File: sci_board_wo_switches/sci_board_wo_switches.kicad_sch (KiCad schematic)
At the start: 18 parts

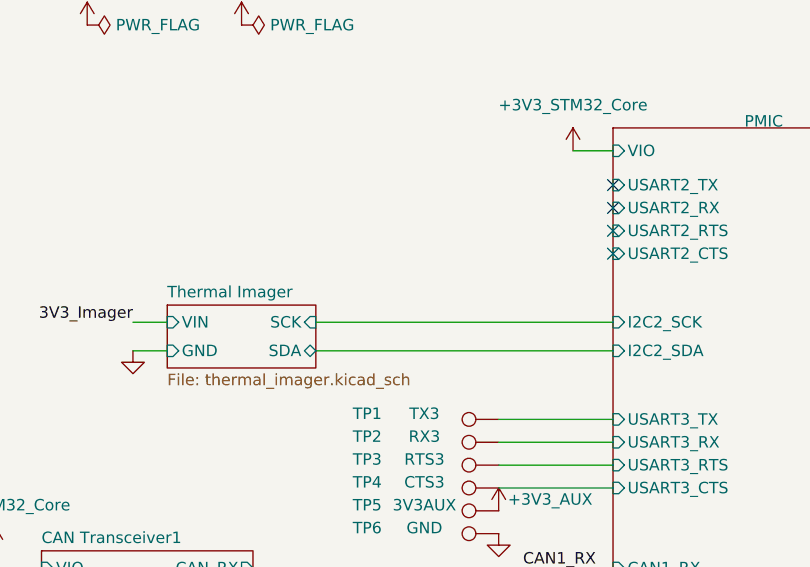
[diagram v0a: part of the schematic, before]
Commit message: bom for SCI
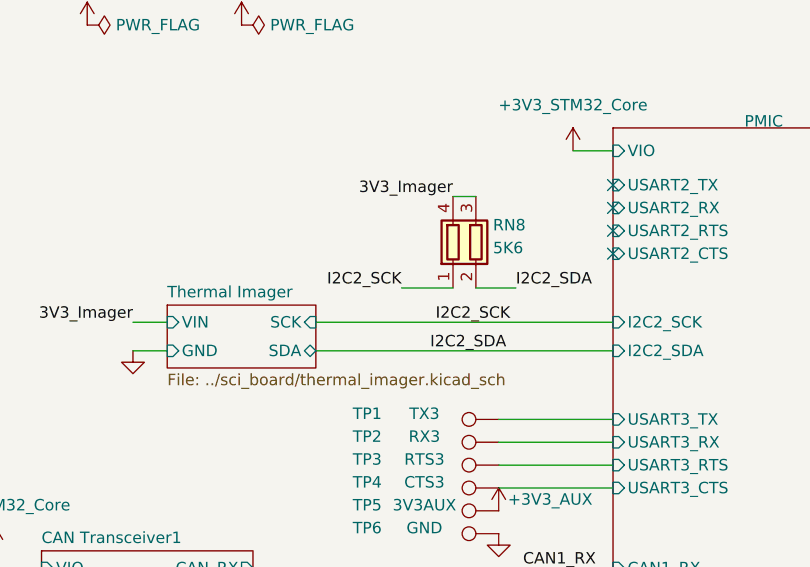
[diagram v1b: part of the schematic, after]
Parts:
- added RN8: 5K6, Resistor_SMD:R_Array_Convex_2x0402, symbol Device:R_Pack02
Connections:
- net 3V3_Imager: now also RN8.3 (R2.2), RN8.4 (R1.2)
- new net I2C2_SCK: RN8.1 (R1.1)
- new net I2C2_SDA: RN8.2 (R2.1)
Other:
- sheet Thermal Imager: file thermal_imager.kicad_sch -> ../sci_board/thermal_imager.kicad_sch
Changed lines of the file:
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@@
 	(wire
 		(pts
+			(xy 64.77 49.53) (xy 70.485 49.53)
+		)
+		(stroke
+			(width 0)
+			(type default)
+		)
+	)
+	(wire
+		(pts
+			(xy 77.47 49.53) (xy 73.025 49.53)
+		)
+		(stroke
+			(width 0)
+			(type default)
+		)
+	)
+	(wire
+		(pts
 			(xy 126.365 105.41) (xy 177.165 105.41)
 		)
@@
 	(wire
 		(pts
+			(xy 70.485 39.37) (xy 73.025 39.37)
+		)
+		(stroke
+			(width 0)
+			(type default)
+		)
+	)
+	(wire
+		(pts
 			(xy 48.26 88.265) (xy 88.265 88.265)
 		)
@@
 		)
 	)
+	(label "I2C2_SCK"
+		(at 76.835 53.34 180)
+		(effects
+			(font
+				(size 1.27 1.27)
+			)
+			(justify right bottom)
+		)
+	)
 	(label "3V3_Cameras"
 		(at 155.575 64.135 180)
@@
 		)
 	)
+	(label "I2C2_SDA"
+		(at 67.945 56.515 0)
+		(effects
+			(font
+				(size 1.27 1.27)
+			)
+			(justify left bottom)
+		)
+	)
 	(label "CAN2_STB"
 		(at 86.36 106.68 180)
@@
 		)
 	)
+	(label "I2C2_SCK"
+		(at 64.77 49.53 180)
+		(effects
+			(font
+				(size 1.27 1.27)
+			)
+			(justify right bottom)
+		)
+	)
 	(label "3V3_Imager"
 		(at 34.925 128.27 180)
@@
 		)
 	)
+	(label "3V3_Imager"
+		(at 70.485 39.37 180)
+		(effects
+			(font
+				(size 1.27 1.27)
+			)
+			(justify right bottom)
+		)
+	)
 	(label "CAN2_H"
 		(at 22.225 109.855 180)
@@
 		)
 	)
+	(label "I2C2_SDA"
+		(at 77.47 49.53 0)
+		(effects
+			(font
+				(size 1.27 1.27)
+			)
+			(justify left bottom)
+		)
+	)
 	(symbol
 		(lib_id "power:+3V3")
@@
 	)
 	(symbol
+		(lib_id "Device:R_Pack02")
+		(at 73.025 44.45 0)
+		(unit 1)
+		(exclude_from_sim no)
+		(in_bom yes)
+		(on_board yes)
+		(dnp no)
+		(property "Reference" "RN8"
+			(at 74.93 42.545 0)
+			(effects
+				(font
+					(size 1.27 1.27)
+				)
+				(justify left)
+			)
+		)
+		(property "Value" "5K6"
+			(at 74.93 45.085 0)
+			(effects
+				(font
+					(size 1.27 1.27)
+				)
+				(justify left)
+			)
+		)
+		(property "Footprint" "Resistor_SMD:R_Array_Convex_2x0402"
+			(at 77.47 44.45 90)
+			(effects
+				(font
+					(size 1.27 1.27)
+				)
+				(hide yes)
+			)
+		)
+		(property "Datasheet" "~"
+			(at 73.025 44.45 0)
+			(effects
+				(font
+					(size 1.27 1.27)
+				)
+				(hide yes)
+			)
+		)
+		(property "Description" "2 resistor network, parallel topology"
+			(at 73.025 44.45 0)
+			(effects
+				(font
+					(size 1.27 1.27)
+				)
+				(hide yes)
+			)
+		)
+		(pin "3"
+		)
+		(pin "1"
+		)
+		(pin "4"
+		)
+		(pin "2"
+		)
+		(instances
+			(project "sci_board_wo_switches"
+				(path "/b4b2c88d-f6cd-4e60-862d-e21f68728580"
+					(reference "RN8")
+					(unit 1)
+				)
+			)
+		)
+	)
+	(symbol
 		(lib_id "power:GND")
 		(at 168.275 154.305 0)
@@
 			)
 		)
-		(property "Sheetfile" "thermal_imager.kicad_sch"
+		(property "Sheetfile" "../sci_board/thermal_imager.kicad_sch"
 			(at 38.735 59.0046 0)
 			(effects

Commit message: EPS AVI SCI SCIwoSwitches RF AUX all updated to use RNs. BOMs completed
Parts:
- R1, R2: MANUFACTURER YAGEO -> (none); Manufacturer (none) -> YAGEO; PARTREV RC0402FR-0710KL -> (none); Part Number (none) -> RC0402FR-0710KL
- R3: MANUFACTURER YAGEO -> (none); Manufacturer (none) -> YAGEO; PARTREV RC0402FR-0722RL -> (none); Part Number (none) -> RC0402FR-0722RL
- R4: MANUFACTURER YAGEO -> (none); Manufacturer (none) -> YAGEO; PARTREV RC0402FR-07100KL -> (none); Part Number (none) -> RC0402FR-07100KL
- R5: MANUFACTURER YAGEO -> (none); Manufacturer (none) -> YAGEO; PARTREV RC0402FR-07330KL -> (none); Part Number (none) -> RC0402FR-07330KL
- RN1, RN3, RN8: Manufacturer (none) -> Panasonic; Part Number (none) -> EXB-24V562JX; Tolerance (none) -> 5
- RN2: Manufacturer (none) -> Panasonic; Part Number (none) -> EXB-24V220JX; Tolerance (none) -> 5
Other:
- sheet Aux Power Switch 3V3: file i2c_aux_power_switch.kicad_sch -> ../sci_board/i2c_aux_power_switch.kicad_sch
- sheet Flash1: file flash.kicad_sch -> ../sci_board/flash.kicad_sch
- sheet Flash2: file flash.kicad_sch -> ../sci_board/flash.kicad_sch

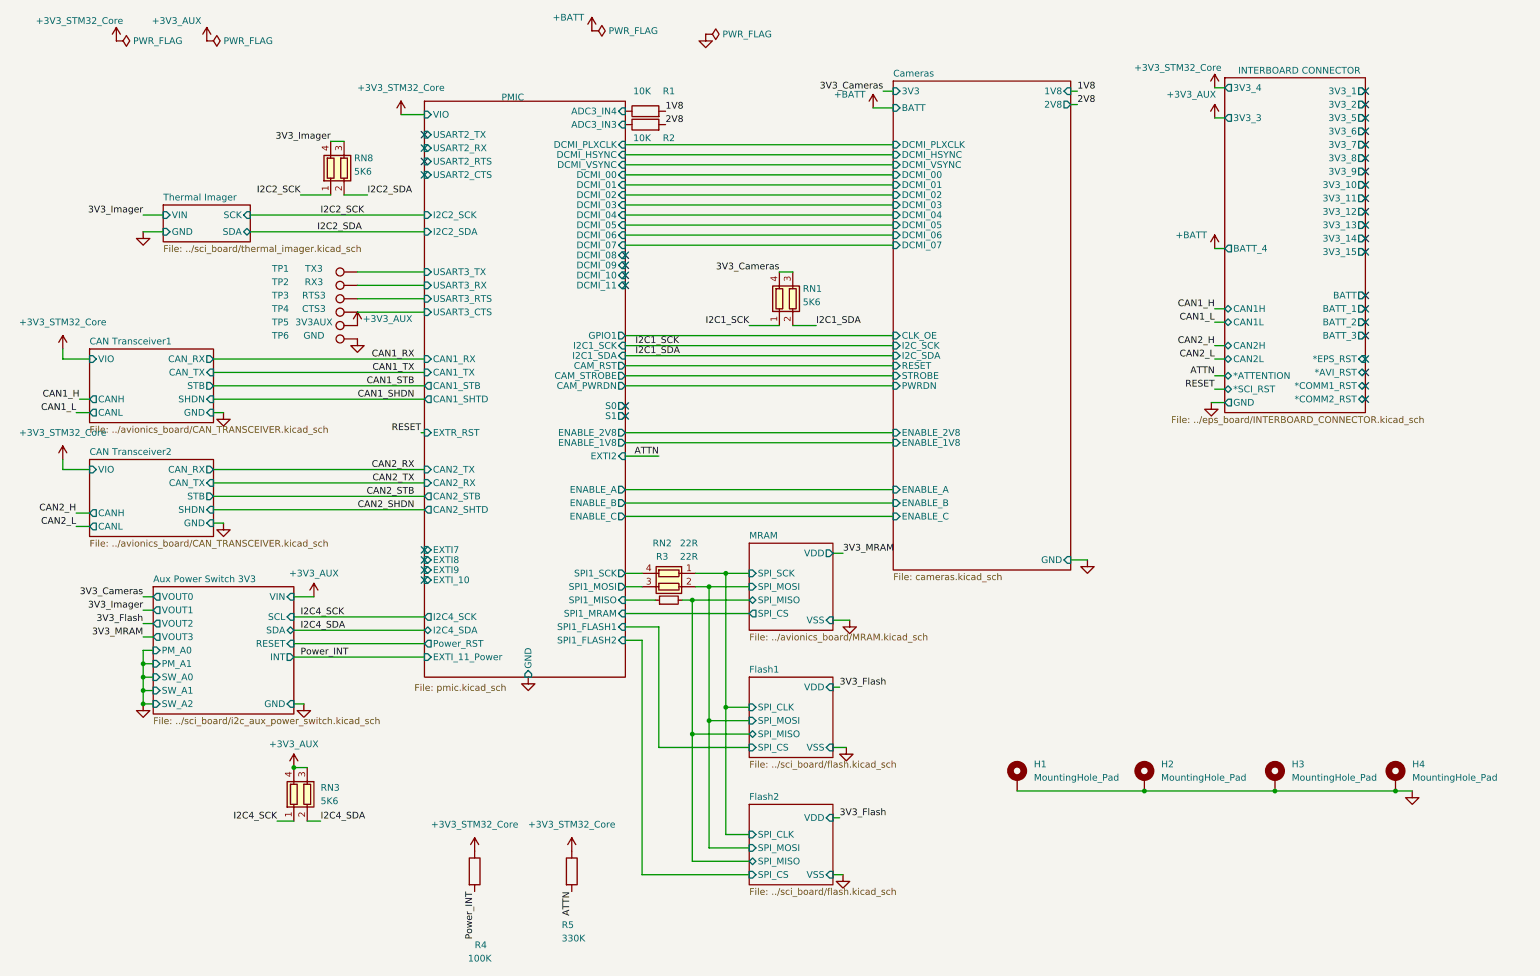
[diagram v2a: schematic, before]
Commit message: sorting out pullups on resets and attention. replace reset with RN where possible. Introduce CN to save some parts
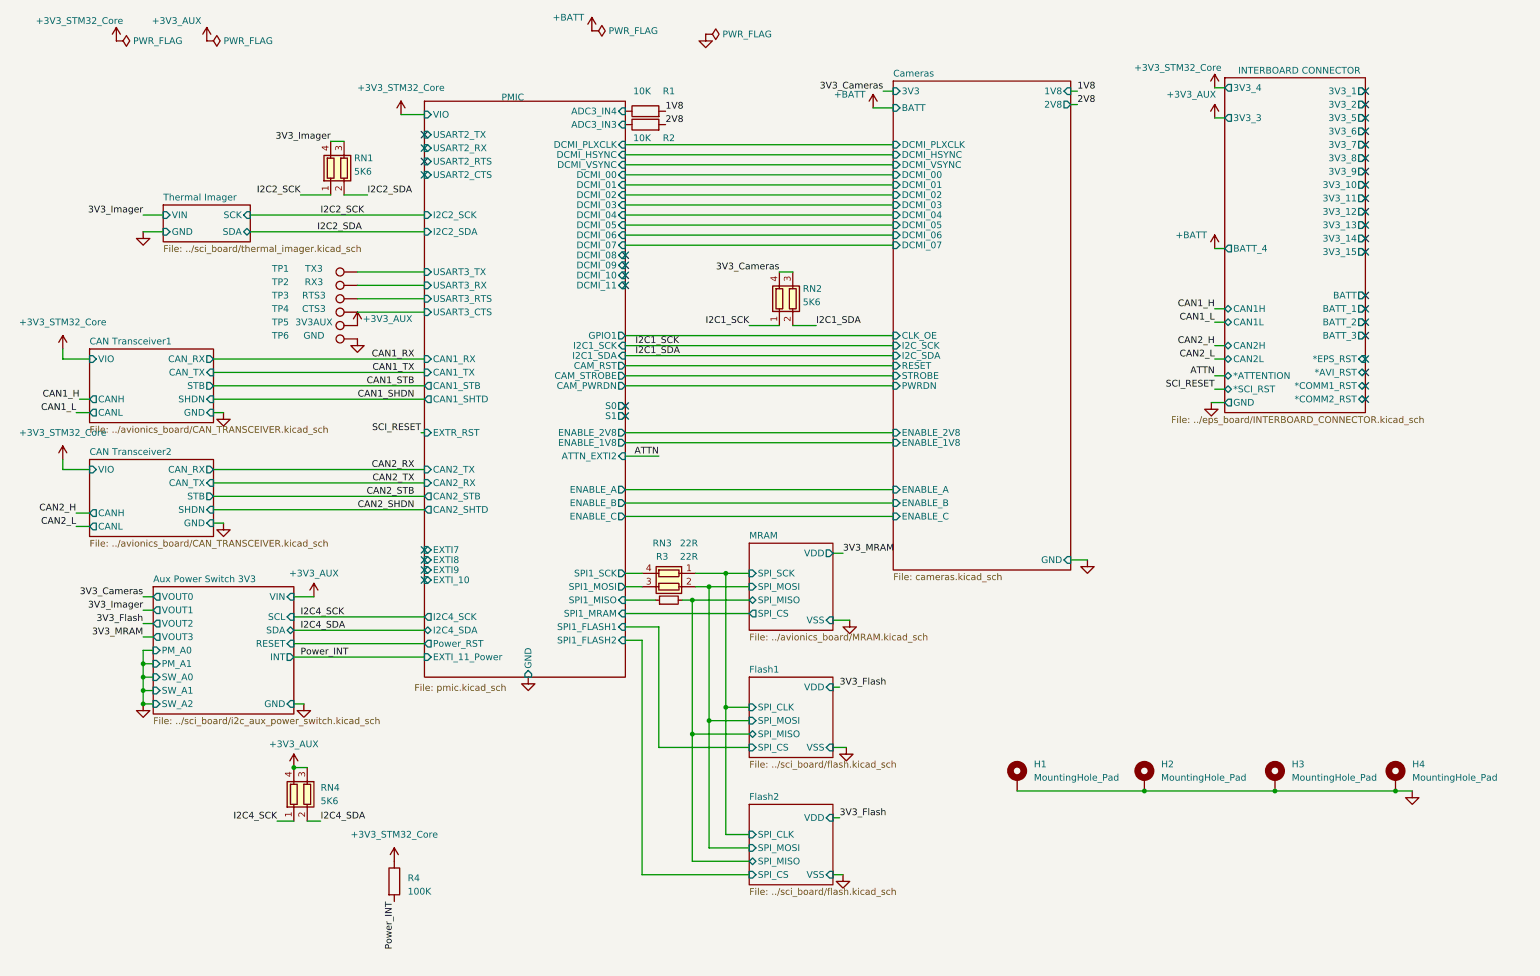
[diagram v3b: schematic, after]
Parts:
- removed R5: 330K, Resistor_SMD:R_0402_1005Metric_Pad0.72x0.64mm_HandSolder, symbol Device:R
- renumbered RN8 to RN1, RN1 to RN2, RN2 to RN3, RN3 to RN4
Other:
- sheet PMIC ports: added ATTN_EXTI2; removed EXTI2
- moved on the sheet: R4
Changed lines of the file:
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@@
 		)
 	)
-	(label "ATTN"
-		(at 116.205 181.61 270)
-		(effects
-			(font
-				(size 1.27 1.27)
-			)
-			(justify right bottom)
-		)
-	)
 	(label "Power_INT"
-		(at 97.79 181.61 270)
+		(at 82.55 183.515 270)
 		(effects
 			(font
@@
 		)
 	)
-	(label "RESET"
+	(label "SCI_RESET"
 		(at 87.63 94.615 180)
 		(effects
@@
 		)
 	)
-	(label "RESET"
+	(label "SCI_RESET"
 		(at 238.125 86.36 180)
 		(effects
@@
 	(symbol
 		(lib_id "Device:R")
-		(at 97.79 177.8 0)
+		(at 82.55 179.705 0)
 		(unit 1)
 		(exclude_from_sim no)
@@
 		(dnp no)
 		(property "Reference" "R4"
-			(at 97.79 191.77 0)
+			(at 85.09 179.07 0)
 			(effects
 				(font
@@
 		)
 		(property "Value" "100K"
-			(at 96.52 194.31 0)
+			(at 85.09 181.61 0)
 			(effects
 				(font
@@
 		)
 		(property "Footprint" "Resistor_SMD:R_0402_1005Metric_Pad0.72x0.64mm_HandSolder"
-			(at 96.012 177.8 90)
+			(at 80.772 179.705 90)
 			(effects
 				(font
@@
 		)
 		(property "Datasheet" "https://www.yageo.com/upload/media/product/app/datasheet/rchip/pyu-rt_1-to-0.01_rohs_l.pdf"
-			(at 97.79 177.8 0)
+			(at 82.55 179.705 0)
 			(effects
 				(font
@@
 		)
 		(property "Description" "Resistor"
-			(at 97.79 177.8 0)
+			(at 82.55 179.705 0)
 			(effects
 				(font
@@
 		)
 		(property "Note" "pullup/pulldown"
-			(at 97.79 177.8 0)
+			(at 82.55 179.705 0)
 			(effects
 				(font
@@
 		)
 		(property "Tolerance" "1"
-			(at 97.79 177.8 0)
+			(at 82.55 179.705 0)
 			(effects
 				(font
@@
 		)
 		(property "Manufacturer" "YAGEO"
-			(at 97.79 177.8 0)
+			(at 82.55 179.705 0)
 			(effects
 				(font
@@
 		)
 		(property "Part Number" "RC0402FR-07100KL"
-			(at 97.79 177.8 0)
+			(at 82.55 179.705 0)
 			(effects
 				(font
@@
 		(dnp no)
 		(fields_autoplaced yes)
-		(property "Reference" "RN3"
+		(property "Reference" "RN4"
 			(at 68.58 161.9249 0)
 			(effects
@@
 			(project ""
 				(path "/b4b2c88d-f6cd-4e60-862d-e21f68728580"
-					(reference "RN3")
+					(reference "RN4")
 					(unit 1)
 				)
@@
 		(dnp no)
 		(fields_autoplaced yes)
-		(property "Reference" "#PWR029"
+		(property "Reference" "#PWR028"
 			(at 167.64 184.785 0)
 			(effects
@@
 			(project "sci_board"
 				(path "/b4b2c88d-f6cd-4e60-862d-e21f68728580"
-					(reference "#PWR029")
+					(reference "#PWR028")
 					(unit 1)
 				)
@@
 		(on_board yes)
 		(dnp no)
-		(property "Reference" "RN2"
+		(property "Reference" "RN3"
 			(at 133.35 115.57 90)
 			(effects
@@
 			(project "sci_board"
 				(path "/b4b2c88d-f6cd-4e60-862d-e21f68728580"
-					(reference "RN2")
+					(reference "RN3")
 					(unit 1)
 				)
@@
 	(symbol
 		(lib_id "power:+3V3")
-		(at 97.79 173.99 0)
+		(at 82.55 175.895 0)
 		(unit 1)
 		(exclude_from_sim no)
@@
 		(fields_autoplaced yes)
 		(property "Reference" "#PWR027"
-			(at 97.79 177.8 0)
+			(at 82.55 179.705 0)
 			(effects
 				(font
@@
 		)
 		(property "Value" "+3V3_STM32_Core"
-			(at 97.79 168.91 0)
+			(at 82.55 170.815 0)
 			(effects
 				(font
@@
 		)
 		(property "Footprint" ""
-			(at 97.79 173.99 0)
+			(at 82.55 175.895 0)
 			(effects
 				(font
@@
 		)
 		(property "Datasheet" ""
-			(at 97.79 173.99 0)
+			(at 82.55 175.895 0)
 			(effects
 				(font
@@
 		)
 		(property "Description" "Power symbol creates a global label with name \"+3V3\""
-			(at 97.79 173.99 0)
+			(at 82.55 175.895 0)
 			(effects
 				(font
@@
 		(on_board yes)
 		(dnp no)
-		(property "Reference" "RN8"
+		(property "Reference" "RN1"
 			(at 74.93 42.545 0)
 			(effects
@@
 			(project "sci_board_wo_switches"
 				(path "/b4b2c88d-f6cd-4e60-862d-e21f68728580"
-					(reference "RN8")
+					(reference "RN1")
 					(unit 1)
 				)
@@
 		(on_board yes)
 		(dnp no)
-		(property "Reference" "RN1"
+		(property "Reference" "RN2"
 			(at 160.02 67.31 0)
 			(effects
@@
 			(project ""
 				(path "/b4b2c88d-f6cd-4e60-862d-e21f68728580"
-					(reference "RN1")
+					(reference "RN2")
 					(unit 1)
 				)
@@
 	)
 	(symbol
-		(lib_id "Device:R")
-		(at 116.205 177.8 0)
-		(unit 1)
-		(exclude_from_sim no)
-		(in_bom yes)
-		(on_board yes)
-		(dnp no)
-		(property "Reference" "R5"
-			(at 114.3 187.96 0)
-			(effects
-				(font
-					(size 1.27 1.27)
-				)
-				(justify left)
-			)
-		)
-		(property "Value" "330K"
-			(at 114.3 190.5 0)
-			(effects
-				(font
-					(size 1.27 1.27)
-				)
-				(justify left)
-			)
-		)
-		(property "Footprint" "Resistor_SMD:R_0402_1005Metric_Pad0.72x0.64mm_HandSolder"
-			(at 114.427 177.8 90)
-			(effects
-				(font
-					(size 1.27 1.27)
-				)
-				(hide yes)
-			)
-		)
-		(property "Datasheet" "https://www.yageo.com/upload/media/product/products/datasheet/rchip/PYu-RC_Group_51_RoHS_L_12.pdf"
-			(at 116.205 177.8 0)
-			(effects
-				(font
-					(size 1.27 1.27)
-				)
-				(hide yes)
-			)
-		)
-		(property "Description" "Resistor"
-			(at 116.205 177.8 0)
-			(effects
-				(font
-					(size 1.27 1.27)
-				)
-				(hide yes)
-			)
-		)
-		(property "Note" "generic pullup/down"
-			(at 116.205 177.8 0)
-			(effects
-				(font
-					(size 1.27 1.27)
-				)
-				(hide yes)
-			)
-		)
-		(property "Tolerance" "1"
-			(at 116.205 177.8 0)
-			(effects
-				(font
-					(size 1.27 1.27)
-				)
-				(hide yes)
-			)
-		)
-		(property "Manufacturer" "YAGEO"
-			(at 116.205 177.8 0)
-			(effects
-				(font
-					(size 1.27 1.27)
-				)
-				(hide yes)
-			)
-		)
-		(property "Part Number" "RC0402FR-07330KL"
-			(at 116.205 177.8 0)
-			(effects
-				(font
-					(size 1.27 1.27)
-				)
-				(hide yes)
-			)
-		)
-		(pin "2"
-		)
-		(pin "1"
-		)
-		(instances
-			(project ""
-				(path "/b4b2c88d-f6cd-4e60-862d-e21f68728580"
-					(reference "R5")
-					(unit 1)
-				)
-			)
-		)
-	)
-	(symbol
-		(lib_id "power:+3V3")
-		(at 116.205 173.99 0)
-		(unit 1)
-		(exclude_from_sim no)
-		(in_bom yes)
-		(on_board yes)
-		(dnp no)
-		(fields_autoplaced yes)
-		(property "Reference" "#PWR028"
-			(at 116.205 177.8 0)
-			(effects
-				(font
-					(size 1.27 1.27)
-				)
-				(hide yes)
-			)
-		)
-		(property "Value" "+3V3_STM32_Core"
-			(at 116.205 168.91 0)
-			(effects
-				(font
-					(size 1.27 1.27)
-				)
-			)
-		)
-		(property "Footprint" ""
-			(at 116.205 173.99 0)
-			(effects
-				(font
-					(size 1.27 1.27)
-				)
-				(hide yes)
-			)
-		)
-		(property "Datasheet" ""
-			(at 116.205 173.99 0)
-			(effects
-				(font
-					(size 1.27 1.27)
-				)
-				(hide yes)
-			)
-		)
-		(property "Description" "Power symbol creates a global label with name \"+3V3\""
-			(at 116.205 173.99 0)
-			(effects
-				(font
-					(size 1.27 1.27)
-				)
-				(hide yes)
-			)
-		)
-		(pin "1"
-		)
-		(instances
-			(project "sci_board"
-				(path "/b4b2c88d-f6cd-4e60-862d-e21f68728580"
-					(reference "#PWR028")
-					(unit 1)
-				)
-			)
-		)
-	)
-	(symbol
 		(lib_id "power:+3V3")
 		(at 63.5 158.115 0)
@@
 			)
 		)
-		(pin "EXTI2" input
-			(at 126.365 99.06 0)
-			(effects
-				(font
-					(size 1.27 1.27)
-				)
-				(justify right)
-			)
-		)
 		(pin "SPI1_SCK" output
 			(at 126.365 121.285 0)
@@
 			(effects
 				(font
+					(size 1.27 1.27)
+				)
+				(justify right)
+			)
+		)
+		(pin "ATTN_EXTI2" input
+			(at 126.365 99.06 0)
+			(effects
+				(font

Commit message: cleanup pullups for reset and schmitt trigger for reset; select available thermal NTCs for avi board and use chip for voltage dividers
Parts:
- RN1, RN2, RN3, RN4: footprint Resistor_SMD:R_Array_Convex_2x0402 -> Common:R_Array_Convex_2x0402_widepads
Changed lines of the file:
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@@
 			)
 		)
-		(property "Footprint" "Resistor_SMD:R_Array_Convex_2x0402"
+		(property "Footprint" "Common:R_Array_Convex_2x0402_widepads"
 			(at 70.485 163.195 90)
 			(effects
@@
 			)
 		)
-		(property "Footprint" "Resistor_SMD:R_Array_Convex_2x0402"
+		(property "Footprint" "Common:R_Array_Convex_2x0402_widepads"
 			(at 134.62 128.27 90)
 			(effects
@@
 			)
 		)
-		(property "Footprint" "Resistor_SMD:R_Array_Convex_2x0402"
+		(property "Footprint" "Common:R_Array_Convex_2x0402_widepads"
 			(at 77.47 44.45 90)
 			(effects
@@
 			)
 		)
-		(property "Footprint" "Resistor_SMD:R_Array_Convex_2x0402"
+		(property "Footprint" "Common:R_Array_Convex_2x0402_widepads"
 			(at 162.56 69.215 90)
 			(effects

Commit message: checked BOM for sci wo switches
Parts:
- removed R1, R2: 10K, Resistor_SMD:R_0402_1005Metric_Pad0.72x0.64mm_HandSolder, symbol Device:R
- added R3: 330K, Resistor_SMD:R_0402_1005Metric_Pad0.72x0.64mm_HandSolder, symbol Device:R
- added RN1: 10K, Common:R_Array_Convex_2x0402_widepads, symbol Device:R_Pack02
- renumbered R3 to R1, R4 to R2, RN1 to RN2, RN2 to RN3, RN3 to RN4, RN4 to RN5
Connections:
- net +3V3_STM32_Core: now also R3.1
- net 1V8: now also RN1.2 (R2.1)
- net 2V8: now also RN1.1 (R1.1)
- net ATTN: now also R3.2
- net PMIC/ADC3_IN3: now also RN1.4 (R1.2)
- net PMIC/ADC3_IN4: now also RN1.3 (R2.2)
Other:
- sheet Cameras ports: added I2C_RST; removed none
- sheet PMIC ports: added I2C2_RST; removed none
- moved on the sheet: R2
